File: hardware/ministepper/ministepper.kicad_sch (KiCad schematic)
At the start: 11 parts, among them U1 STM32G071G8U6, U2 TMC2130-LA, U3 TMC2130-LA, U4 SIT3088EEUA

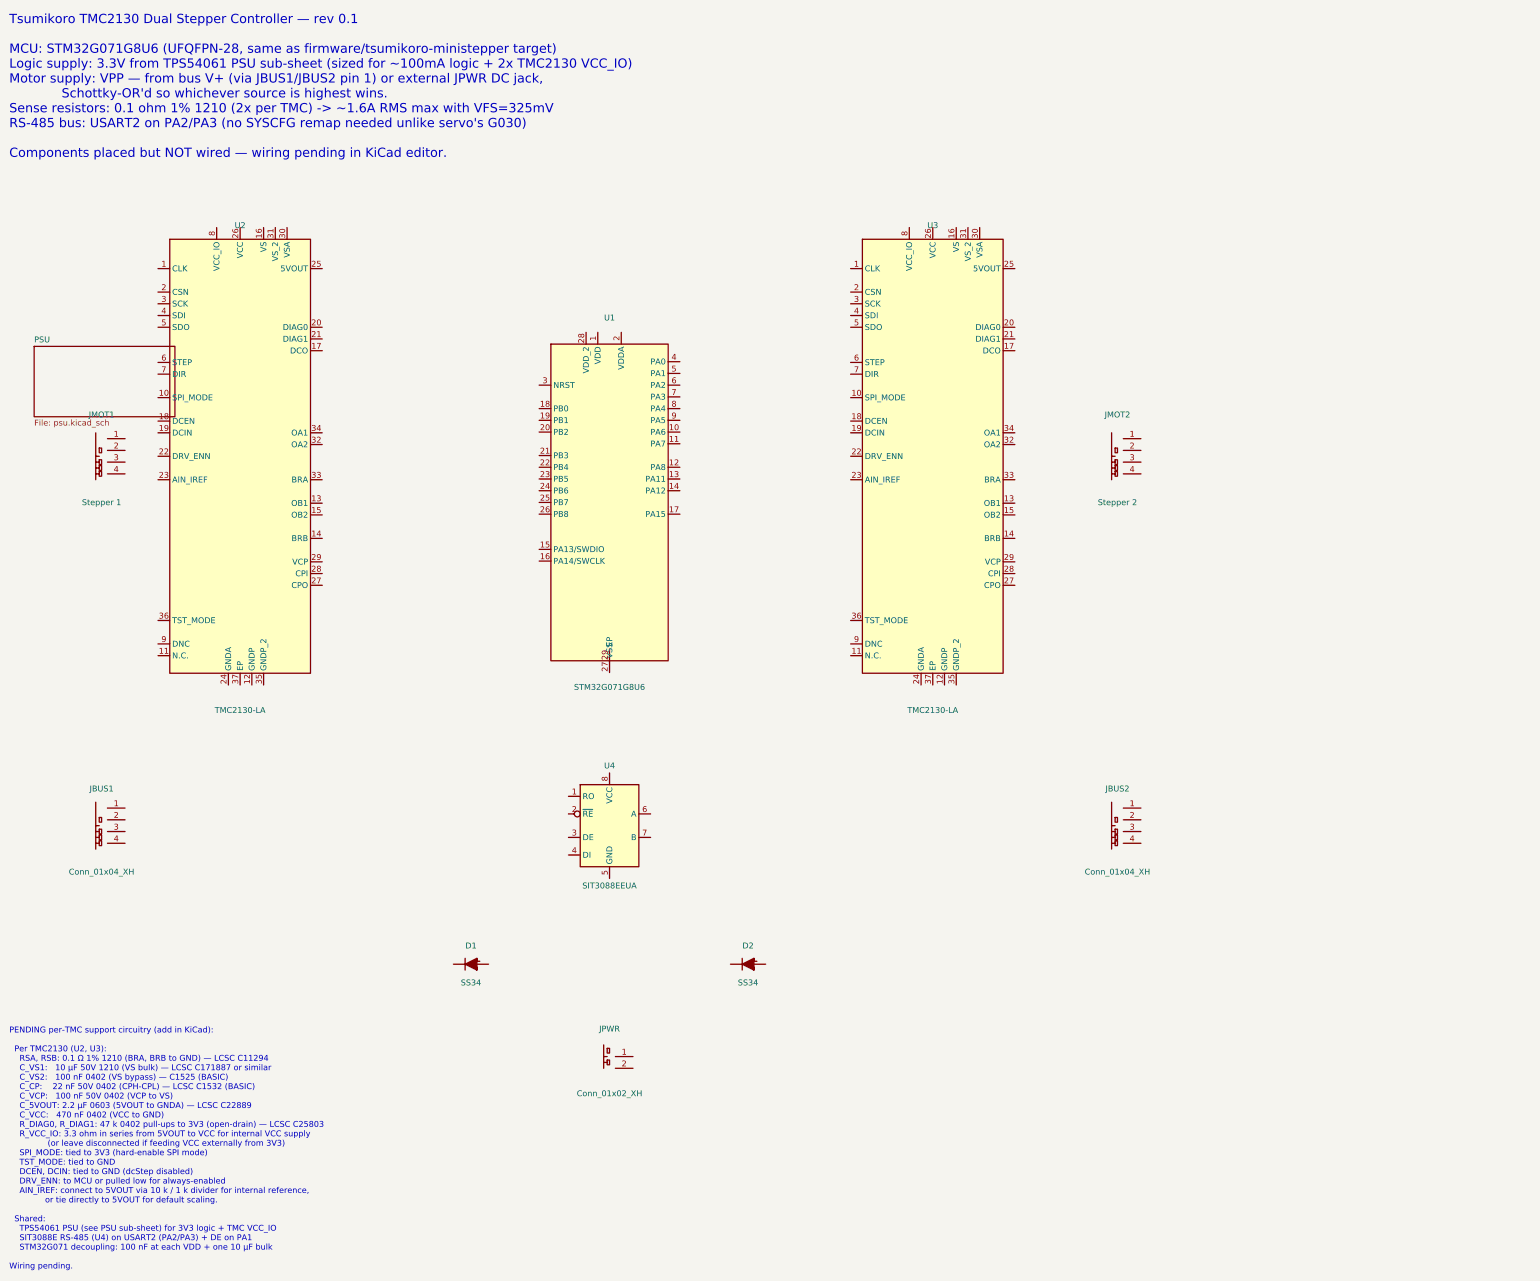
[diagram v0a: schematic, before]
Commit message: ministepper: motor connectors (JMOT1, JMOT2) switch to vertical JST-XH
Was S4B-XH-A horizontal (right-angle, LCSC C157925) — now B4B-XH-A
vertical (top-mount, LCSC C595709, B4B-XH-A-R(LF)(SN), red housing
version, ~$0.08). The vertical variant keeps the motor cables exiting
straight up, which is usually more natural for stepper wiring vs the
board-edge horizontal style.

Bus connectors (JBUS1, JBUS2) and the optional external-power input
(JPWR) remain horizontal S*B-XH-A for board-edge cable exit.

Also regenerates docs + JLCPCB package.
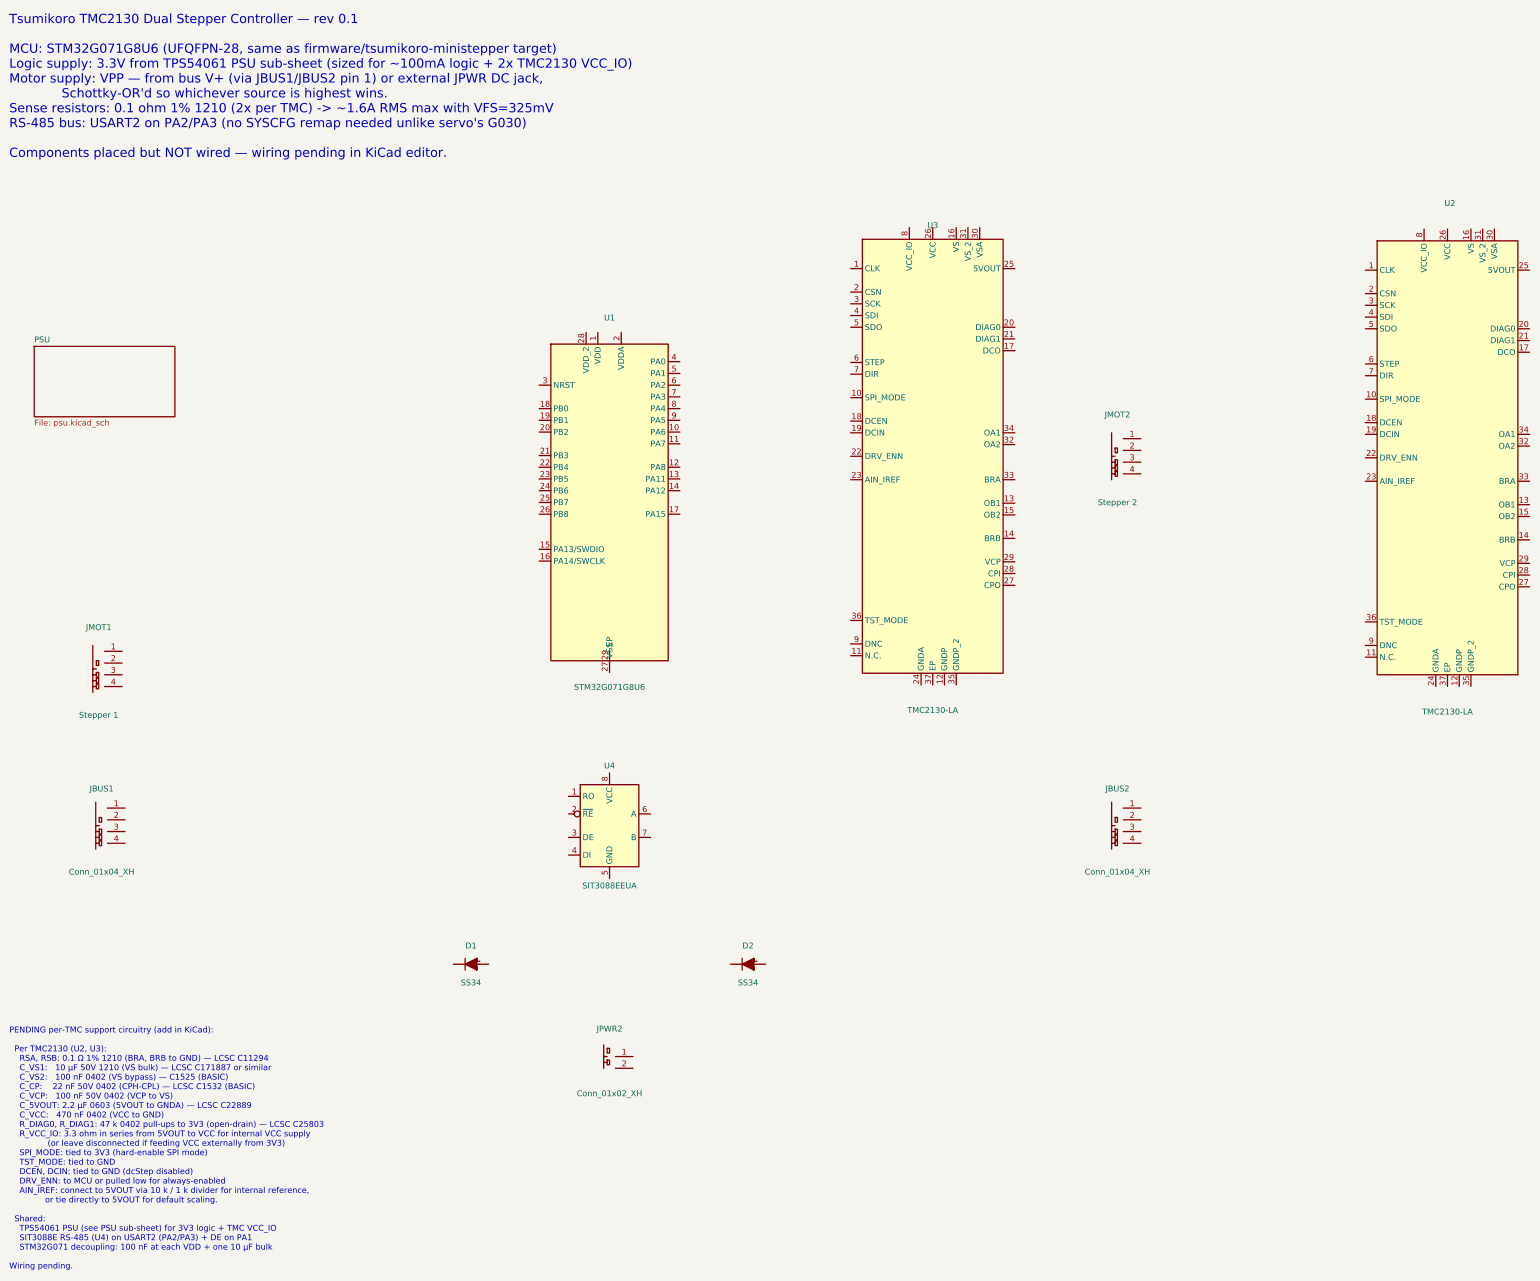
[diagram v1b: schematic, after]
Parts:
- removed JPWR: Conn_01x02_XH, Connector_JST:JST_XH_S2B-XH-A_1x02_P2.50mm_Horizontal, symbol Connector_Generic:Conn_01x02
- added JPWR2: Conn_01x02_XH, Connector_JST:JST_XH_S2B-XH-A_1x02_P2.50mm_Horizontal, symbol Connector_Generic:Conn_01x02
- JMOT1, JMOT2: footprint Connector_JST:JST_XH_S4B-XH-A_1x04_P2.50mm_Horizontal -> Connector_JST:JST_XH_B4B-XH-A_1x04_P2.50mm_Vertical; LCSC C157925 -> C595709; MPN S4B-XH-A(LF)(SN) -> B4B-XH-A-R(LF)(SN)

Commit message: ministepper: refactor as multi-channel design via reusable sub-sheet
New hardware/ministepper/stepper_channel.kicad_sch contains a single
TMC2130 stepper channel — one TMC2130-LA plus all the per-driver support
passives from the datasheet:

  - RSA/RSB   0.1 ohm 1% 1210 sense (standard, populated)
  - RSA_M/RSB_M  0.68 ohm 1% 1210 sense (micro / 28BYJ-48 variant, DNP)
  - C_VS_BULK  10 uF 50V 1210 motor-rail bulk
  - C_VS       100 nF 0402 VS HF bypass
  - C_VSA      100 nF 0402 VSA filter
  - C_CP       22 nF 50V 0402 charge-pump flying cap (CPH<->CPL)
  - C_VCP      100 nF 50V 0402 charge-pump storage (VCP->VS)
  - C_5VOUT    2.2 uF 6.3V 0603 internal LDO output
  - C_VCC      100 nF 0402 digital VCC
  - C_AIN      100 nF 0402 AIN_IREF reference filter
  - R_DIAG1    47 k 0402 DIAG1 open-drain pull-up
  - U1         tsumikoro:TMC2130-LA

Plus hierarchical ports for the signal interface:
  SCK, MOSI, MISO, DRV_ENN (shared across both channels)
  CS, STEP, DIR (per-channel inputs)
  DIAG1 (per-channel output)
  MOT_A+/-, MOT_B+/- (motor outputs to connector)

Power nets (+3V3, VPP, GND) are global — no hier port needed.

Root schematic (ministepper.kicad_sch) now:
  - Dropped the duplicate U2/U3 TMC2130 instances and the
    "PENDING per-TMC support circuitry" annotation
  - Shows two hierarchical sheet instances pointing at the SAME file:
    "Stepper 1" and "Stepper 2". KiCad auto-renumbers refs per instance.
  - Continues to reuse psu.kicad_sch for the 3V3 logic PSU

Components remain unwired — user wires one channel's sub-sheet in KiCad,
then connects the two sheet instances to the shared SPI bus, per-channel
step/dir/cs/diag nets, and motor connectors on the root sheet.

Updated hardware/ministepper/docs/README.md with the sheet architecture
diagram and the full hierarchical-port table.
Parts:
- removed U2, U3: TMC2130-LA, Package_DFN_QFN:QFN-36-1EP_5x6mm_P0.5mm_EP3.6x4.6mm, symbol tsumikoro:TMC2130-LA
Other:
- added sheet Stepper 1 (stepper_channel.kicad_sch)
- added sheet Stepper 2 (stepper_channel.kicad_sch)
- note removed: "PENDING per-TMC support circuitry (add in KiCad): Per TMC2130 (U2, U3): RSA, RSB: 0.1 Ω 1% 1210 (BRA, BRB to GND) — LCSC C11294 C_VS1: 10 µF 50V 1210 (VS bulk) — LCSC C171887 or similar C_VS2: 100 nF 0402 (VS bypass) — C1525 (BASIC) C_CP: 22 nF 50V 0402 (CPH-CPL) — LCSC C1532 (BASIC) C_VCP: 100 nF 50V 0402 (VCP to VS) C_5VOUT: 2.2 µF 0603 (5VOUT to GNDA) — LCSC C22889 C_VCC: 470 nF 0402 (VCC to G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"

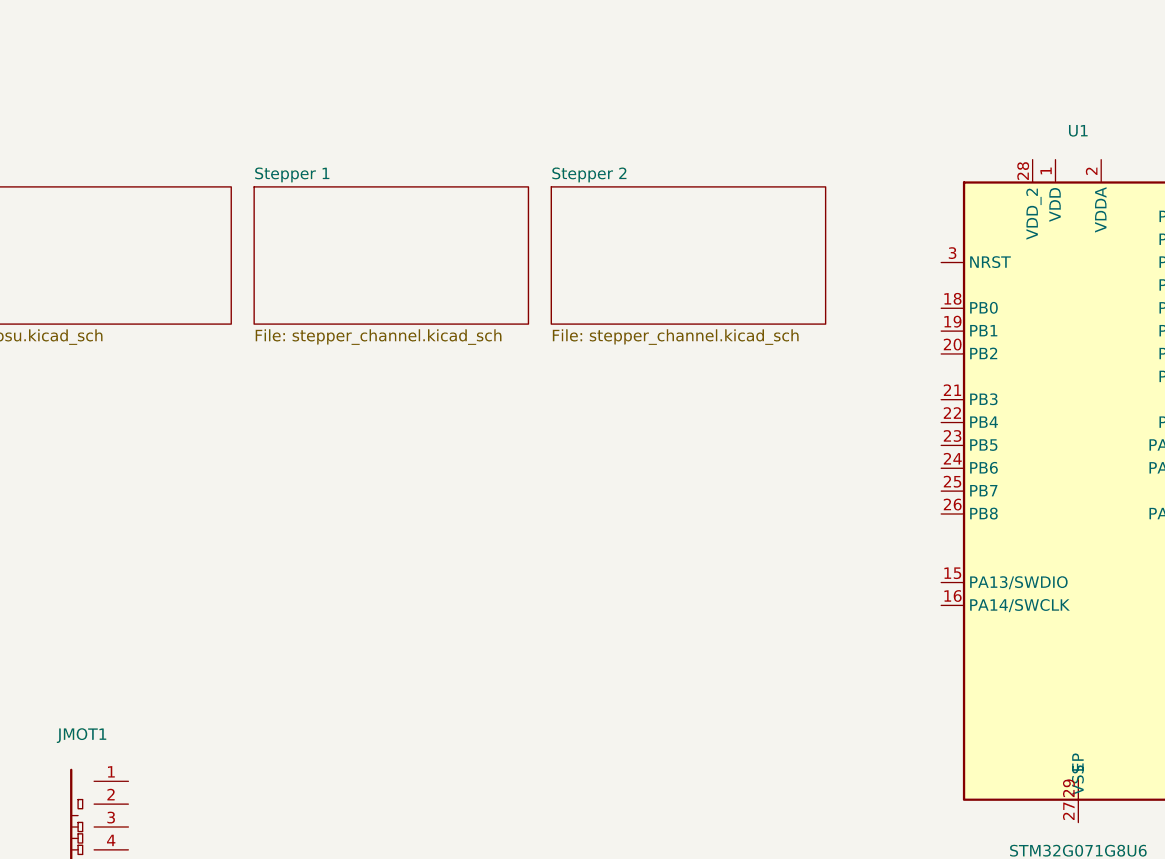
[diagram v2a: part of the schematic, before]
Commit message: ministepper: stepper sub-sheet blocks now expose hier pins
Each of the two stepper-channel sheet instances on the root schematic
is resized to 40x30 mm and given explicit hierarchical pins along its
edges:

  Left edge (signal interface to MCU):
    SCK, MOSI (input)
    MISO (output)
    CS, STEP, DIR, DRV_ENN (input)
    DIAG1 (output)

  Right edge (motor interface to JMOTx connector):
    MOT_A+, MOT_A- (output)
    MOT_B+, MOT_B- (output)

Previously the sheet blocks were just rectangles — you couldn't actually
wire to them on the root sheet because the hier labels in
stepper_channel.kicad_sch hadn't been imported as pins on the parent
sheet symbol. Now when you open ministepper.kicad_sch you see each
stepper channel as a block with 8 pins on the left and 4 on the right,
ready to wire to the MCU SPI bus + per-axis control signals + motor
connector.

Also regenerates docs + JLCPCB package. No BOM changes (sheets don't
have refs).
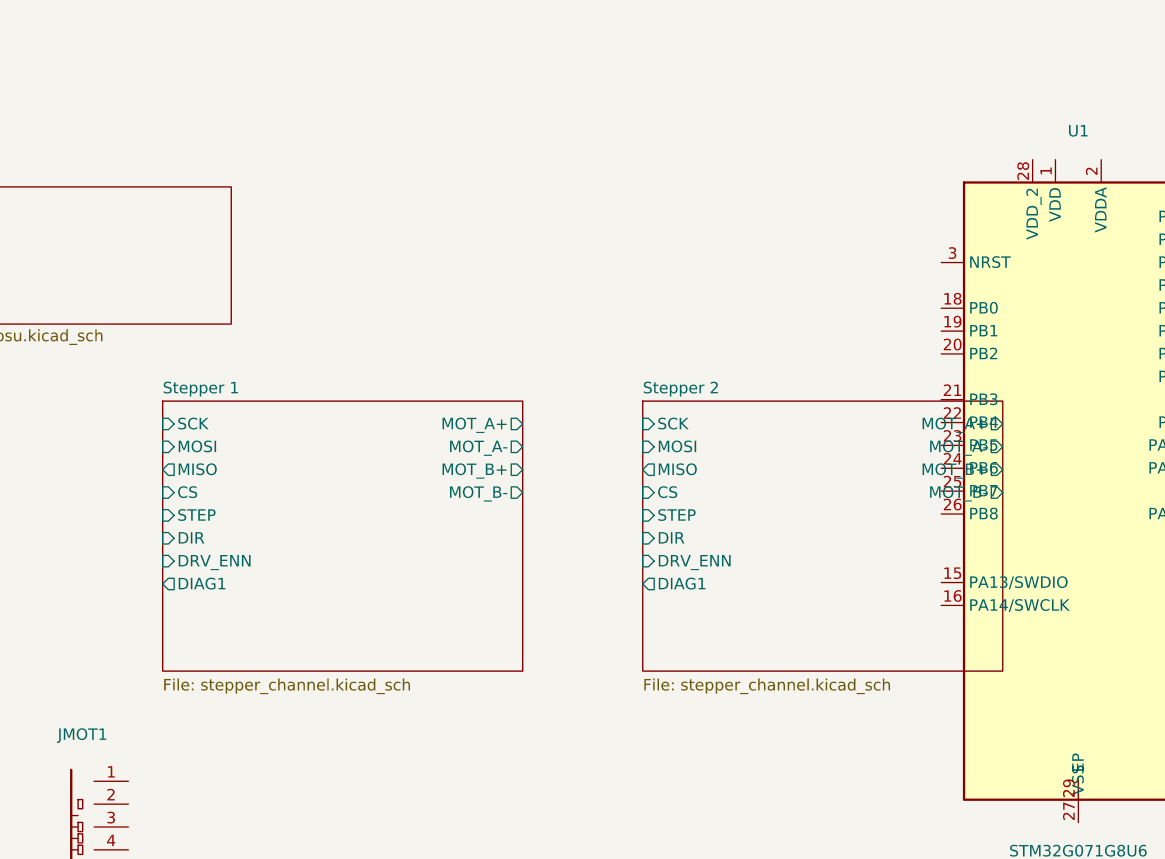
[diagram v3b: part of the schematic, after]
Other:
- sheet Stepper 1 ports: added CS, DIAG1, DIR, DRV_ENN, MISO, MOSI, MOT_A+, MOT_A-, MOT_B+, MOT_B-, SCK, STEP; removed none
- sheet Stepper 2 ports: added CS, DIAG1, DIR, DRV_ENN, MISO, MOSI, MOT_A+, MOT_A-, MOT_B+, MOT_B-, SCK, STEP; removed none
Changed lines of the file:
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@@
 	)
 	(sheet
-		(at 58.42 76.2)
-		(size 30.48 15.24)
+		(at 48.26 100)
+		(size 40 30)
 		(fields_autoplaced yes)
 		(stroke (width 0.1524) (type solid))
 		(fill (color 225 240 255 1))
-		(property "Sheetname" "Stepper 1" (at 58.42 75.4884 0) (effects (font (size 1.27 1.27)) (justify left bottom)))
-		(property "Sheetfile" "stepper_channel.kicad_sch" (at 58.42 92.0146 0) (effects (font (size 1.27 1.27)) (justify left top)))
+		(property "Sheetname" "Stepper 1"
+			(at 48.26 99.2884 0)
+			(effects (font (size 1.27 1.27)) (justify left bottom))
+		)
+		(property "Sheetfile" "stepper_channel.kicad_sch"
+			(at 48.26 130.8146 0)
+			(effects (font (size 1.27 1.27)) (justify left top))
+		)
+		(pin "SCK" input
+			(at 48.26 102.54 180)
+			(effects (font (size 1.27 1.27)) (justify right))
+		)
+		(pin "MOSI" input
+			(at 48.26 105.08000000000001 180)
+			(effects (font (size 1.27 1.27)) (justify right))
+		)
+		(pin "MISO" output
+			(at 48.26 107.62 180)
+			(effects (font (size 1.27 1.27)) (justify right))
+		)
+		(pin "CS" input
+			(at 48.26 110.16000000000001 180)
+			(effects (font (size 1.27 1.27)) (justify right))
+		)
+		(pin "STEP" input
+			(at 48.26 112.7 180)
+			(effects (font (size 1.27 1.27)) (justify right))
+		)
+		(pin "DIR" input
+			(at 48.26 115.24000000000001 180)
+			(effects (font (size 1.27 1.27)) (justify right))
+		)
+		(pin "DRV_ENN" input
+			(at 48.26 117.78 180)
+			(effects (font (size 1.27 1.27)) (justify right))
+		)
+		(pin "DIAG1" output
+			(at 48.26 120.32000000000001 180)
+			(effects (font (size 1.27 1.27)) (justify right))
+		)
+		(pin "MOT_A+" output
+			(at 88.25999999999999 102.54 0)
+			(effects (font (size 1.27 1.27)) (justify left))
+		)
+		(pin "MOT_A-" output
+			(at 88.25999999999999 105.08000000000001 0)
+			(effects (font (size 1.27 1.27)) (justify left))
+		)
+		(pin "MOT_B+" output
+			(at 88.25999999999999 107.62 0)
+			(effects (font (size 1.27 1.27)) (justify left))
+		)
+		(pin "MOT_B-" output
+			(at 88.25999999999999 110.16000000000001 0)
+			(effects (font (size 1.27 1.27)) (justify left))
+		)
 	)
 	(sheet
-		(at 91.44 76.2)
-		(size 30.48 15.24)
+		(at 101.6 100)
+		(size 40 30)
 		(fields_autoplaced yes)
 		(stroke (width 0.1524) (type solid))
 		(fill (color 225 255 225 1))
-		(property "Sheetname" "Stepper 2" (at 91.44 75.4884 0) (effects (font (size 1.27 1.27)) (justify left bottom)))
-		(property "Sheetfile" "stepper_channel.kicad_sch" (at 91.44 92.0146 0) (effects (font (size 1.27 1.27)) (justify left top)))
+		(property "Sheetname" "Stepper 2"
+			(at 101.6 99.2884 0)
+			(effects (font (size 1.27 1.27)) (justify left bottom))
+		)
+		(property "Sheetfile" "stepper_channel.kicad_sch"
+			(at 101.6 130.8146 0)
+			(effects (font (size 1.27 1.27)) (justify left top))
+		)
+		(pin "SCK" input
+			(at 101.6 102.54 180)
+			(effects (font (size 1.27 1.27)) (justify right))
+		)
+		(pin "MOSI" input
+			(at 101.6 105.08000000000001 180)
+			(effects (font (size 1.27 1.27)) (justify right))
+		)
+		(pin "MISO" output
+			(at 101.6 107.62 180)
+			(effects (font (size 1.27 1.27)) (justify right))
+		)
+		(pin "CS" input
+			(at 101.6 110.16000000000001 180)
+			(effects (font (size 1.27 1.27)) (justify right))
+		)
+		(pin "STEP" input
+			(at 101.6 112.7 180)
+			(effects (font (size 1.27 1.27)) (justify right))
+		)
+		(pin "DIR" input
+			(at 101.6 115.24000000000001 180)
+			(effects (font (size 1.27 1.27)) (justify right))
+		)
+		(pin "DRV_ENN" input
+			(at 101.6 117.78 180)
+			(effects (font (size 1.27 1.27)) (justify right))
+		)
+		(pin "DIAG1" output
+			(at 101.6 120.32000000000001 180)
+			(effects (font (size 1.27 1.27)) (justify right))
+		)
+		(pin "MOT_A+" output
+			(at 141.6 102.54 0)
+			(effects (font (size 1.27 1.27)) (justify left))
+		)
+		(pin "MOT_A-" output
+			(at 141.6 105.08000000000001 0)
+			(effects (font (size 1.27 1.27)) (justify left))
+		)
+		(pin "MOT_B+" output
+			(at 141.6 107.62 0)
+			(effects (font (size 1.27 1.27)) (justify left))
+		)
+		(pin "MOT_B-" output
+			(at 141.6 110.16000000000001 0)
+			(effects (font (size 1.27 1.27)) (justify left))
+		)
 	)
 	(sheet
